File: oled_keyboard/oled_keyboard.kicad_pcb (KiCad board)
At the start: 2 copper layers, 125 x 125 mm, 116 parts, among them J1 Conn_01x20_Socket, J10 Conn_01x20_Socket, J11 Conn_01x20_Socket, J12 Conn_01x20_Socket, J2 Conn_01x20_Socket, J3 Conn_01x20_Socket, J4 Conn_01x20_Socket, J5 Conn_01x20_Socket, J6 Conn_01x20_Socket, J7 Conn_01x20_Socket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

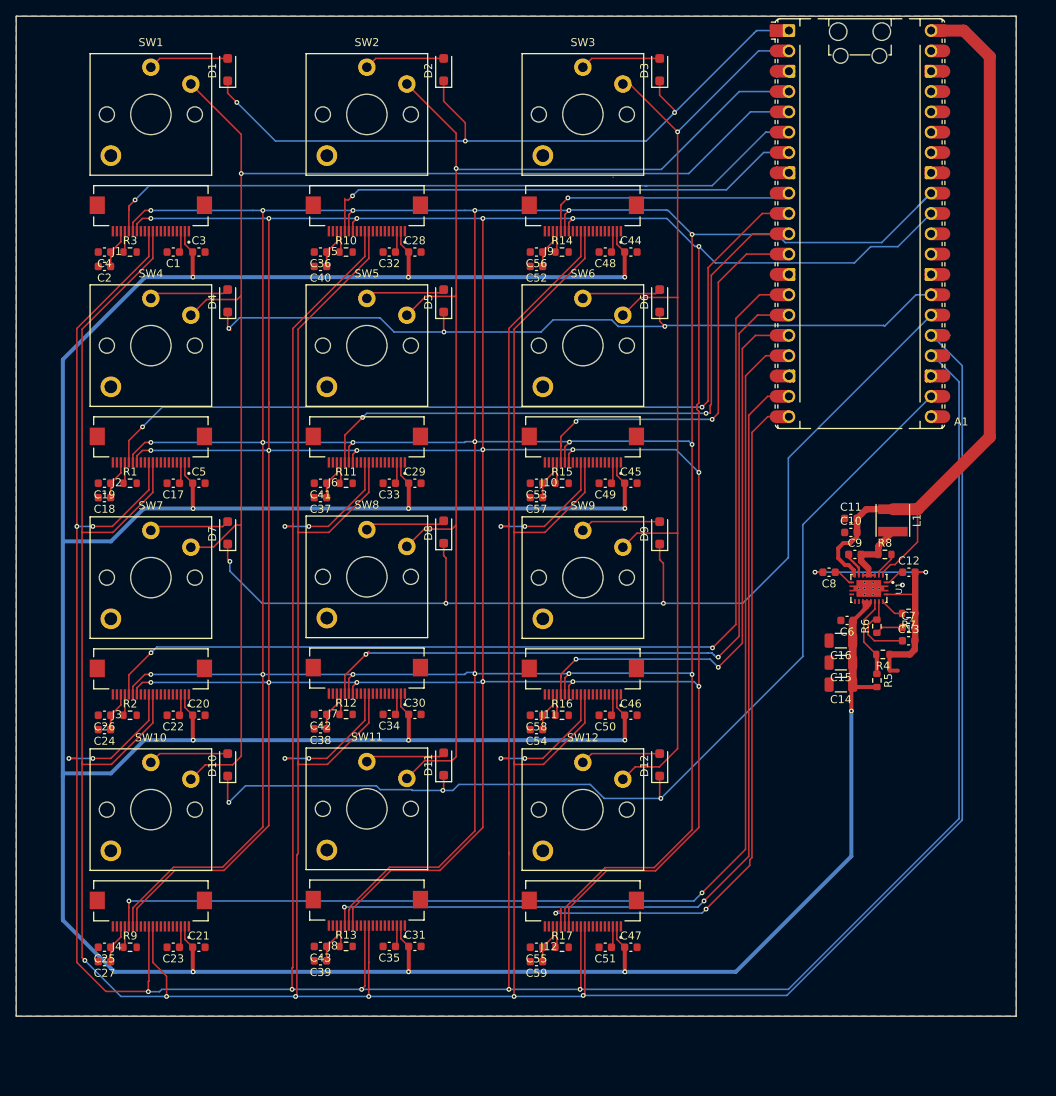
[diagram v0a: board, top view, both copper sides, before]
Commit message: fix: fixed reversed 20pin connector pinout
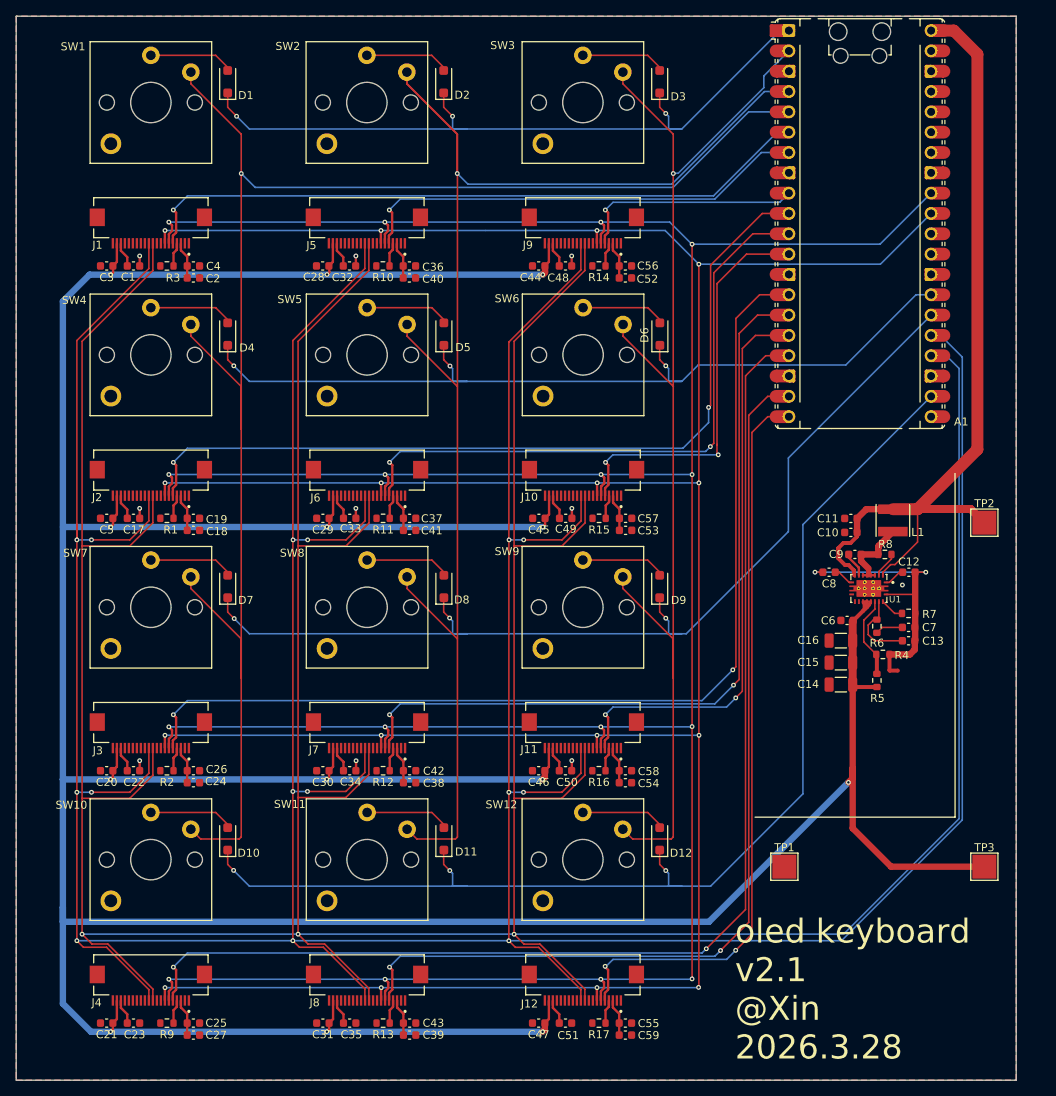
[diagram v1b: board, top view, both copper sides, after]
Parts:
- added TP1: TestPoint, TestPoint:TestPoint_Pad_3.0x3.0mm, F.Cu at (177.9, 136.8)
- added TP2: TestPoint, TestPoint:TestPoint_Pad_3.0x3.0mm, F.Cu at (202.9, 93.8)
- added TP3: TestPoint, TestPoint:TestPoint_Pad_3.0x3.0mm, F.Cu at (202.9, 136.8)
- J1, J10, J11, J12, J2, J3, J4, J5, J6, J7, J8, J9: footprint 20p_connector:HRS_TF31-20S-0.5SH_800_ -> Library:HRS_TF31-20S-0.5SH_800
- moved C31 15.0 mm to (120.2, 156.4), turned to 180 degrees
- moved C47 14.9 mm to (147.2, 156.4), turned to 180 degrees
- moved C21 14.9 mm to (93.2, 156.4), turned to 180 degrees
- moved C43 14.7 mm to (131.0, 156.4), turned to 0 degrees
- moved C25 14.6 mm to (104.0, 156.4), turned to 0 degrees
- moved C55 14.6 mm to (158.0, 156.4), turned to 0 degrees
- moved C39 14.5 mm to (131.0, 157.9), turned to 0 degrees
- moved C27 14.4 mm to (104.0, 157.9), turned to 0 degrees
- moved C59 14.4 mm to (158.0, 157.9), turned to 0 degrees
- moved C30 13.5 mm to (120.2, 124.8), turned to 180 degrees
- moved C46 13.5 mm to (147.2, 124.8), turned to 180 degrees
- moved C20 13.5 mm to (93.2, 124.8), turned to 180 degrees
- moved C42 13.2 mm to (131.0, 124.8), turned to 0 degrees
- moved C26 13.1 mm to (104.0, 124.8), turned to 0 degrees
- moved C58 13.1 mm to (158.0, 124.8), turned to 0 degrees
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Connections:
- A1 pad 37: GND -> unconnected-(A1-3V3_EN-Pad37)
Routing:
- net /DC: track 554.0 -> 409.8 mm, vias 18 -> 16
- net /RES: track 565.6 -> 422.6 mm, vias 18 -> 16
- net VCC: track 509.1 -> 544.5 mm
- net /COL2: track 153.9 -> 187.9 mm
- net /COL1: track 180.5 -> 209.2 mm
- net /SCK: track 593.4 -> 566.1 mm, vias 17 -> 3
- net /COL3: track 128.3 -> 152.4 mm
- net /MOSI: track 593.9 -> 571.9 mm, vias 6 -> 15
- net /ROW4: track 130.3 -> 149.3 mm
- net GND: track 0.00 -> 11.3 mm, vias 1 -> 10
- net /ROW2: track 98.8 -> 108.7 mm
- net VBUS: track 96.3 -> 103.4 mm
- net /CS2: track 62.1 -> 57.4 mm
- net /ROW3: track 130.7 -> 126.2 mm
- net /CS1: track 90.0 -> 85.5 mm
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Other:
- board size 125 x 125 mm -> 125 x 133 mm
- board text added: "oled keyboard v2.1 @Xin 2026.3.28"
